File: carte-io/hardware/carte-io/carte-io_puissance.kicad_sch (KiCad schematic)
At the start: 1 part, among them J2 Conn_01x02

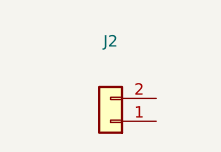
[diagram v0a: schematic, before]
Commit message: Selection de differents connecteurs
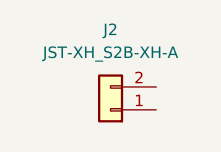
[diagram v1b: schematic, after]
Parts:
- J2: value Conn_01x02 -> JST-XH_S2B-XH-A; footprint Connector_Wuerth:Wuerth_WR-WTB_64800211622_1x02_P1.50mm_Vertical -> Connector_JST:JST_XH_S2B-XH-A_1x02_P2.50mm_Horizontal
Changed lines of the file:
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@@
 	(symbol
 		(lib_id "Connector_Generic:Conn_01x02")
-		(at 29.21 34.29 180)
+		(at 29.21 33.02 180)
 		(unit 1)
 		(exclude_from_sim no)
@@
 		(fields_autoplaced yes)
 		(property "Reference" "J2"
-			(at 29.21 25.4 0)
+			(at 29.21 24.13 0)
 			(effects
 				(font
@@
 			)
 		)
-		(property "Value" "Conn_01x02"
-			(at 29.21 27.94 0)
+		(property "Value" "JST-XH_S2B-XH-A"
+			(at 29.21 26.67 0)
 			(effects
 				(font
 					(size 1.27 1.27)
 				)
-				(hide yes)
 			)
 		)
-		(property "Footprint" "Connector_Wuerth:Wuerth_WR-WTB_64800211622_1x02_P1.50mm_Vertical"
-			(at 29.21 34.29 0)
+		(property "Footprint" "Connector_JST:JST_XH_S2B-XH-A_1x02_P2.50mm_Horizontal"
+			(at 29.21 33.02 0)
 			(effects
 				(font
@@
 		)
 		(property "Datasheet" "~"
-			(at 29.21 34.29 0)
+			(at 29.21 33.02 0)
 			(effects
 				(font
@@
 		)
 		(property "Description" "Generic connector, single row, 01x02, script generated (kicad-library-utils/schlib/autogen/connector/)"
-			(at 29.21 34.29 0)
+			(at 29.21 33.02 0)
 			(effects
 				(font
@@
 			)
 		)
+		(pin "2"
+		)
 		(pin "1"
 		)
-		(pin "2"
-		)
 		(instances
-			(project ""
+			(project "carte-io"
 				(path "/acbeee85-bee7-482c-b859-0ad6bf15d6be/a0428d88-8c4a-4775-8048-a66da608a5ba"
 					(reference "J2")
